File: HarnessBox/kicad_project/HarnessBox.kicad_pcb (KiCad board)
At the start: 2 copper layers, 30.5 x 30.4 mm, 13 parts, among them J1 5018762640, K1 G6K-2G-Y DC5, Q1 DDTC114ECA-7-F, U1 RJ45-DB-101PWB, U2 105450-0101

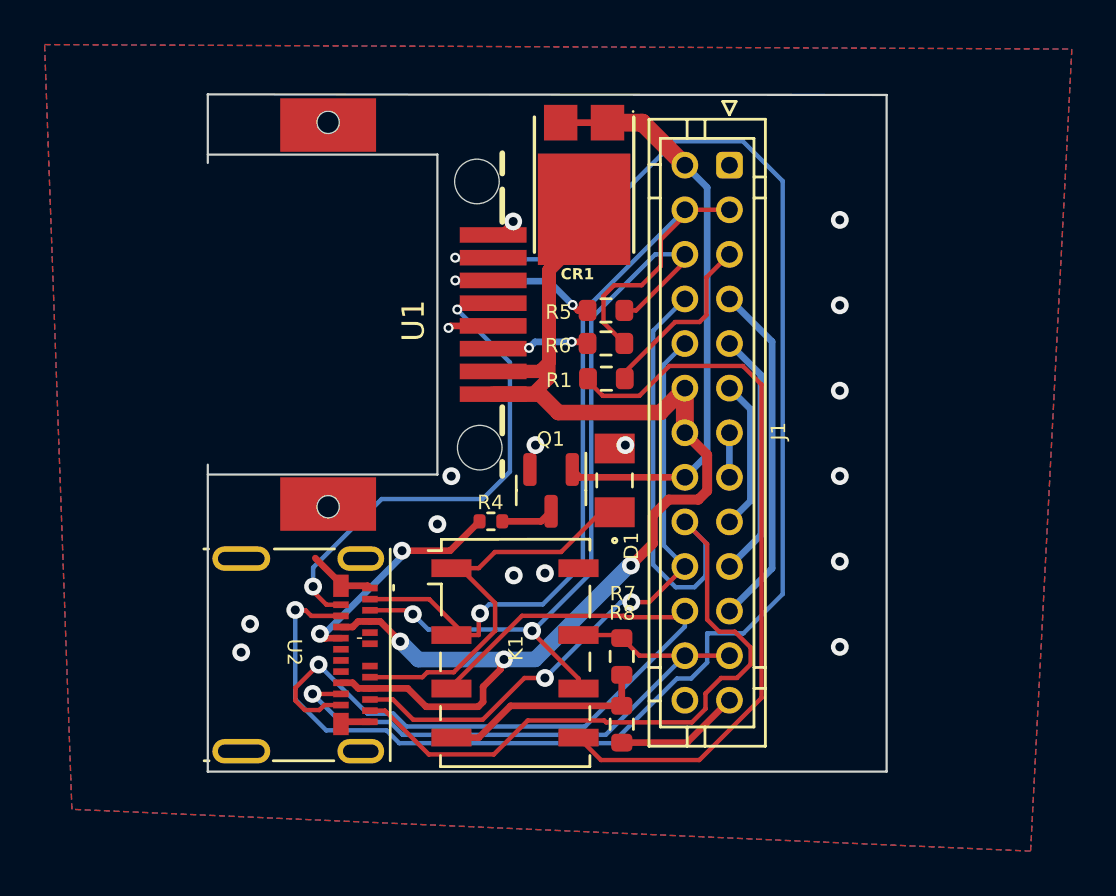
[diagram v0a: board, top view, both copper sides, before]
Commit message: - J533 Harness + STLs - STLs for Harnessbox - STLs for Blackpanda
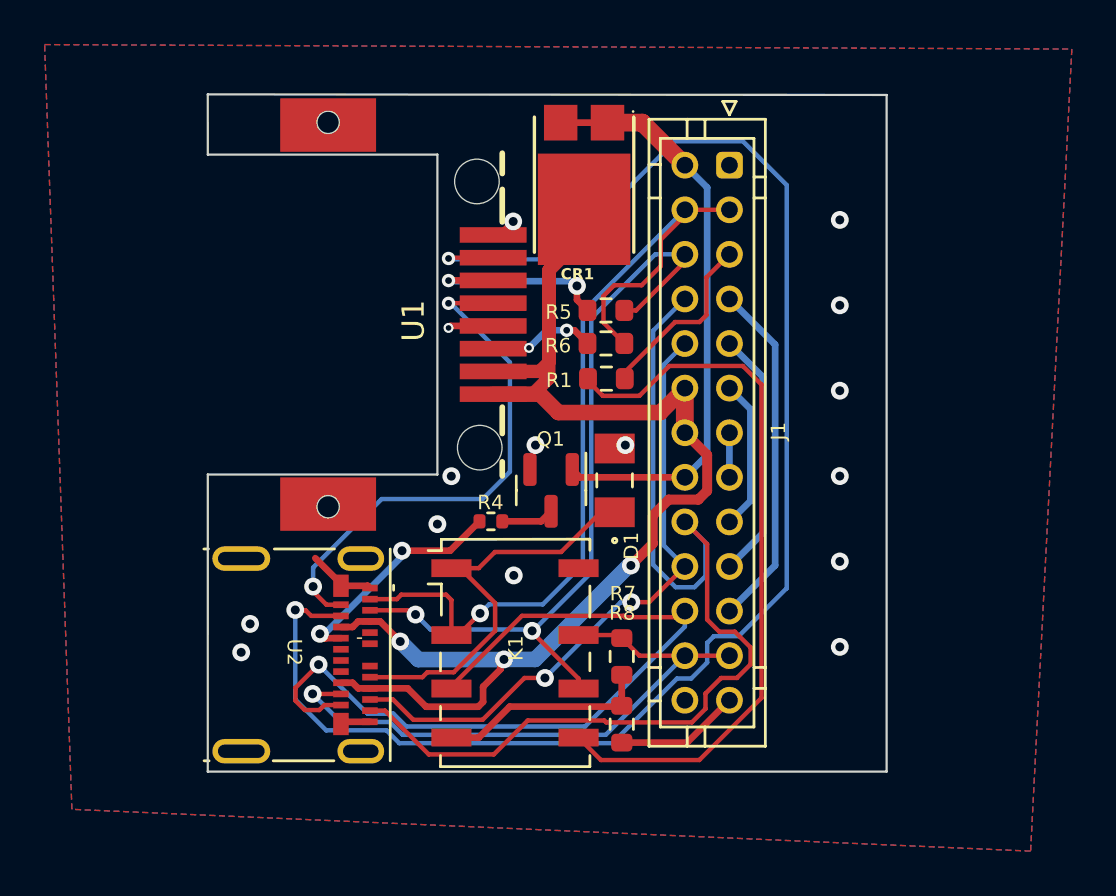
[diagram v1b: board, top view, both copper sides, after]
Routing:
- net +12V: track 62.6 -> 61.4 mm
- net Net-(U1-RX+): track 8.18 -> 9.16 mm
- net CAN3_H: track 23.2 -> 23.9 mm
- net GND: vias 16 -> 15
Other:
- outline, holes or cut-outs redrawn
- board text removed: "by loetkolben"

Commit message: Updated HarnessBox PCB shape
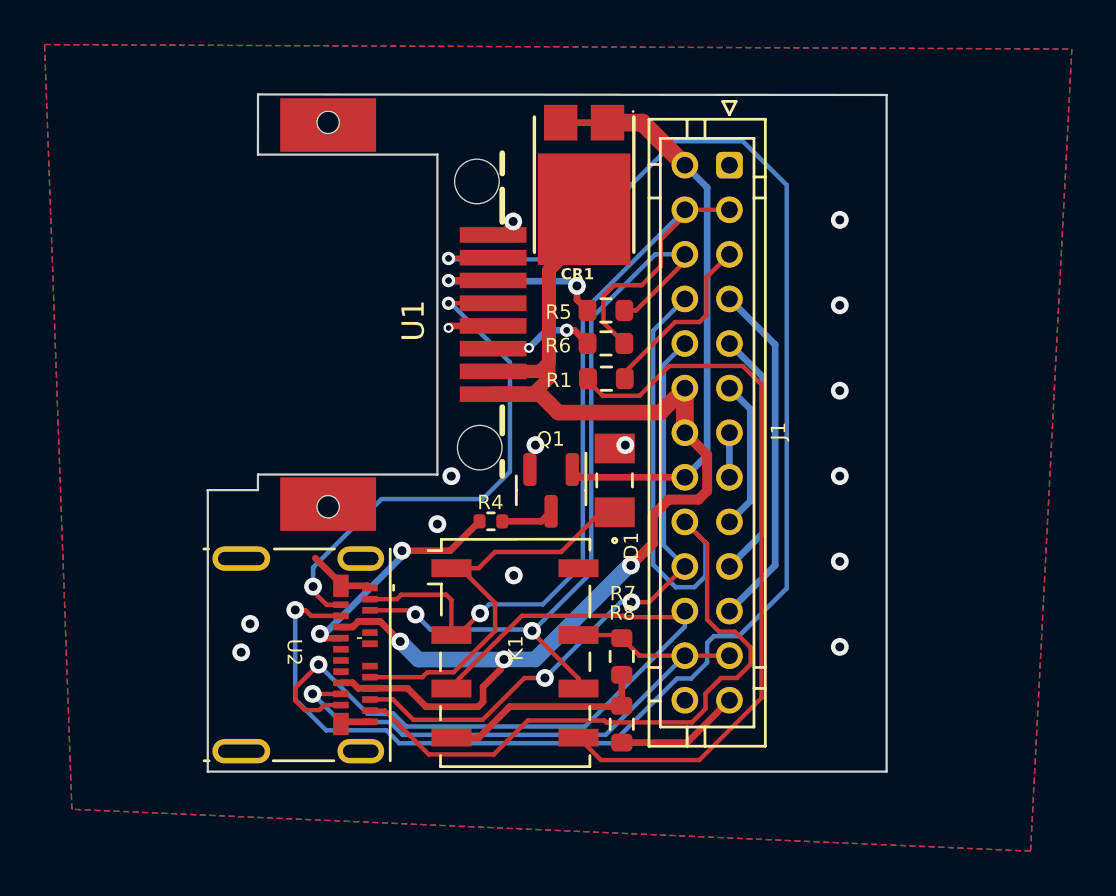
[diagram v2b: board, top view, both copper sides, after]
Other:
- outline, holes or cut-outs redrawn
